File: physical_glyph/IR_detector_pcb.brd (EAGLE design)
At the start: 100 x 80 mm, 37 parts, among them IC1 7805T, IC2 LM339N, U1 MCP6004-I/P

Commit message: Added PCB design
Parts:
- removed IC1: 7805T, linear:TO220H
- added C10, C11, C12, C13: 0.1uF, resistor:C025-024X044
- added D2: 1N4004, diode:DO41-10
- added J1: (no value), SparkFun-Connectors:SCREWTERMINAL-5MM-2
- added J2: (no value), SparkFun-Connectors:1X02
- added Q2: (no value), SparkFun-Sensors:LTR-301
- added R24, R31, R33, R34, R40, R44: 1k, rcl:0204V
- added R25, R30, R32, R38, R41: 10k, rcl:0204V
- added R26, R27, R28, R45, R46: 1M, rcl:0204V
- added R29: 3.9k, rcl:0204V
- added R35, R36, R37, R39: 100k, rcl:0204V
- added R42, R43: 4.7k, rcl:0204V
- added U2: MCP6004-I/P, Microchip_By_element14_Batch_1:DIP254P762X533-14
- C2: value 0.1uF -> 10uF
- moved C2 66.5 mm to (61.0, 24.1), turned to 0 degrees
- moved C1 65.6 mm to (41.9, 14.0), turned to 90 degrees
- moved C9 35.8 mm to (67.3, 44.5), turned to 90 degrees
- moved R8 29.6 mm to (88.9, 58.4)
- moved R4 22.2 mm to (81.3, 53.3)
- moved R7 22.2 mm to (80.0, 58.4)
- moved R23 22.2 mm to (72.4, 52.1)
- moved R11 22.2 mm to (72.4, 57.1)
- moved R22 22.2 mm to (72.4, 54.6)
- moved R6 21.9 mm to (77.5, 53.3)
- moved R5 18.5 mm to (88.9, 53.3)
- moved C3 15.3 mm to (40.6, 48.3)
- moved C6 8.89 mm to (27.9, 72.4)
- moved D1 8.13 mm to (50.8, 47.0)
- moved R1 8.03 mm to (36.8, 48.3)
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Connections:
- removed net VIN: C1.1, IC1.1
- new net 2.5V2: R39.1, R40.2, U2.8, U2.9
- new net COMP_OUT2: IC2.2, R27.1, R29.2, R31.2
- new net GAIN2_IN2: C13.1, R39.2, U2.12
- new net GAIN2_OUT2: C11.2, R42.2, U2.14
- new net GAIN_OUT2: C13.2, R43.2, U2.1
- new net IR_SIGNAL2: C10.1, R33.2, U2.3
- new net MICRO_IN2: J2.2, R30.2, R31.1
- new net N$10: C10.2, Q2.E, R32.1
- new net N$11: D2.A, U2.7
- new net N$12: C12.1, R36.1, R37.2, U2.10
- new net N$13: R24.1, R38.1, U2.2
- new net N$14: R40.1, R41.1, U2.13
- new net N$15: R41.2, R42.1
- new net N$16: R38.2, R43.1
- new net N$17: R34.1, R44.2
- new net N$9: IC2.4, R26.2, R27.2, R28.2, R45.2, R46.2
- new net PEAK_DIODE2: D2.C, R34.2, U2.6
- new net PEAK_IN2: C11.1, R35.2, U2.5
- new net PEAK_OUT2: C2.2, IC2.5, R25.2, R44.1
- net 5V: now also C1.2, J1.1, Q2.C, R26.1, R29.1, R36.2, U2.4; no longer C2.2, IC1.3
- net COMP_OUT: now also IC2.13; no longer IC2.2
- net GND: now also C1.1, C12.2, J1.2, R24.2, R25.1, R28.1, R30.1, R32.2, R33.1, R35.1, R37.1, R45.1, R46.1, U2.11; no longer C1.2, IC1.2
- net MICRO_IN: now also J2.1
- net N$34: now also IC2.10; no longer IC2.4
- net PEAK_OUT: now also IC2.11; no longer IC2.5
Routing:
- net GND: track 184.5 -> 326.2 mm
- net 5V: track 143.2 -> 216.9 mm
- net PEAK_OUT2: track 0.00 -> 44.9 mm
- net MICRO_IN: track 9.67 -> 54.2 mm
- net 2.5V2: track 0.00 -> 40.1 mm
- net IR_SIGNAL2: track 0.00 -> 39.3 mm
- net MICRO_IN2: track 0.00 -> 29.5 mm
- net PEAK_IN2: track 0.00 -> 26.4 mm
- net COMP_OUT2: track 0.00 -> 25.3 mm
- net GAIN2_IN2: track 0.00 -> 24.7 mm
- net N$9: track 0.00 -> 23.3 mm
- net PEAK_DIODE2: track 0.00 -> 17.1 mm
- net GAIN_OUT2: track 0.00 -> 16.5 mm
- net GAIN2_OUT2: track 0.00 -> 15.7 mm
- net N$12: track 0.00 -> 14.5 mm
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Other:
- board size 100 x 80 mm -> 93.7 x 80 mm

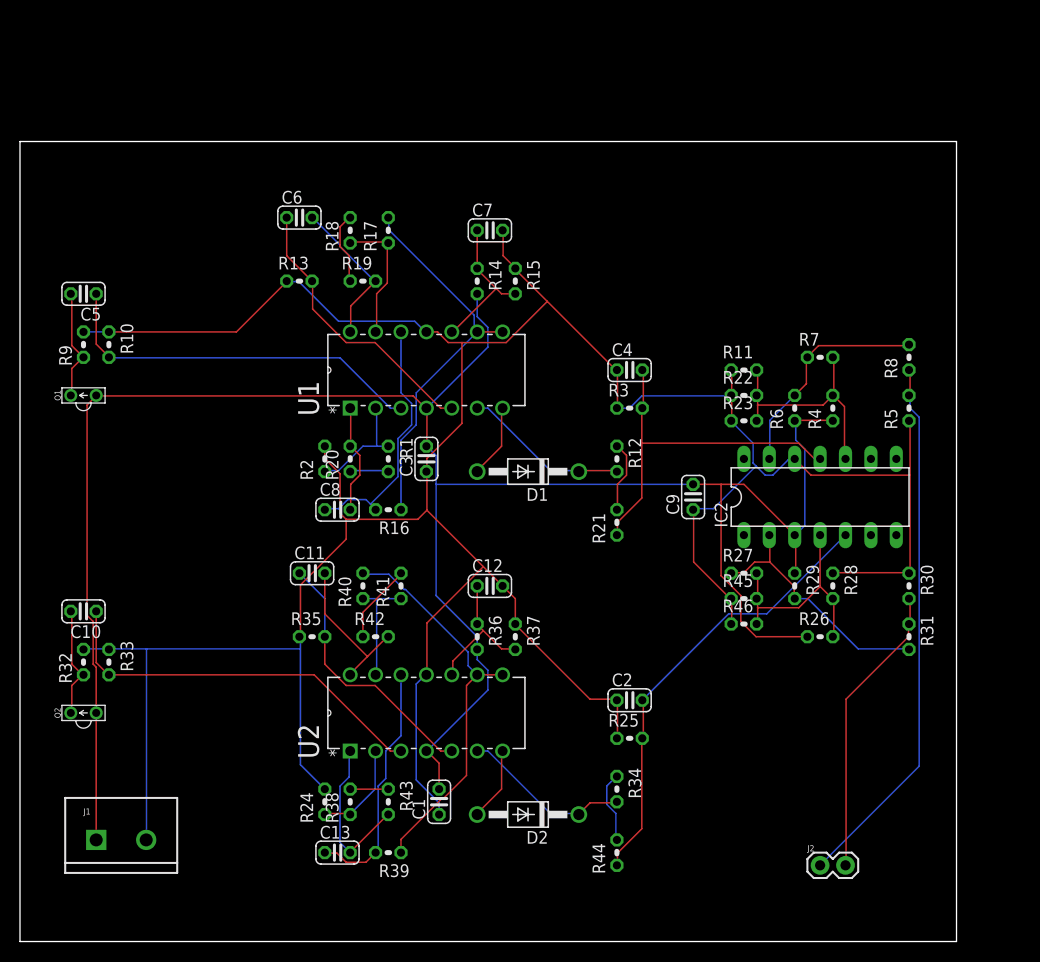
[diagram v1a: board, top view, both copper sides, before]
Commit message: Fixed a long standing regression with the IR circuit
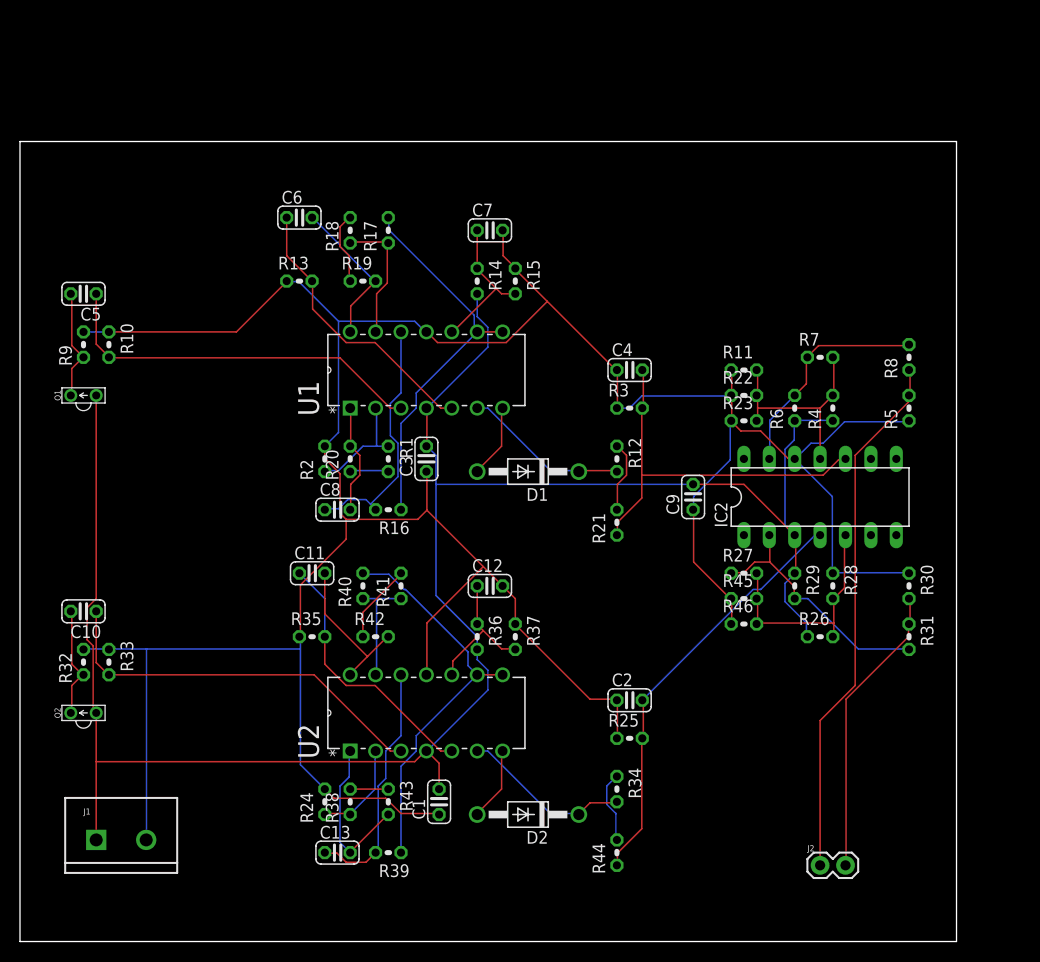
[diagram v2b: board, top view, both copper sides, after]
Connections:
- net N$34: now also IC2.11; no longer IC2.10
- net N$9: now also IC2.5; no longer IC2.4
- net PEAK_OUT: now also IC2.10; no longer IC2.11
- net PEAK_OUT2: now also IC2.4; no longer IC2.5
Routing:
- net 5V: track 216.9 -> 202.7 mm
- net GND: track 326.2 -> 320.3 mm
- net PEAK_OUT: track 36.3 -> 38.8 mm
- net PEAK_OUT2: track 44.9 -> 42.4 mm
- net N$34: track 24.1 -> 22.4 mm
- net MICRO_IN: track 54.2 -> 53.4 mm
